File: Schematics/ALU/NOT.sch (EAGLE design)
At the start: 23 parts

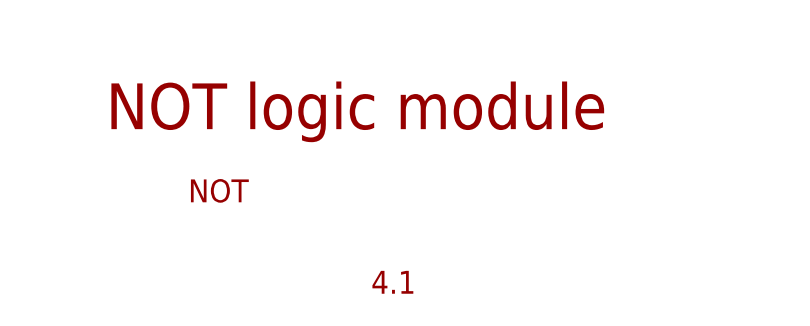
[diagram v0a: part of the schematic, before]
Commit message: Correct page number for NOT
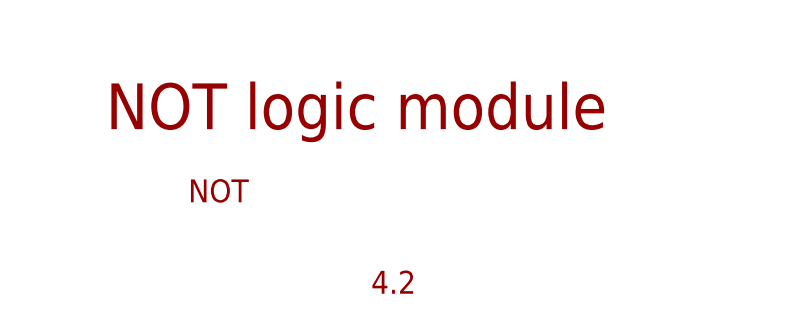
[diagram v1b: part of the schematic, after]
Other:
- note added: "4.2"
- note removed: "4.1"
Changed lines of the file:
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@@
 <text x="166.116" y="25.908" size="5.08" layer="94">NOT logic module</text>
 <text x="175.26" y="17.78" size="2.54" layer="94">NOT</text>
-<text x="195.58" y="7.62" size="2.54" layer="94">4.1</text>
+<text x="195.58" y="7.62" size="2.54" layer="94">4.2</text>
 <text x="259.08" y="7.62" size="2.54" layer="94">1</text>
 </plain>
